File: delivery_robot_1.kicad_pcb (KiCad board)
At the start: 4 copper layers, 100 x 106 mm, 156 parts, among them J1 SWD, J13 Pi 5 link, J14 Pi 5 power, J15 Motor2 encoder, J16 MDD20A PWM2/DIR2/GND, J17 Latch servo, J18 AUX1 Notecard, J19 AUX2 LiDAR, J2 XT30PW-M, J20 AUX3 GNSS, J21 AUX4 IMU, J22 AUX force-on, J4 BOOT0 jumper, J5 Power test points, J6 MDD20A PWM1/DIR1/GND, J7 Motor1 encoder, J8 Expansion header, Q1 SQJ409EP, Q2 DMN63D8L, SW1 RESET, U1 STM32F091RCTx, U10 74LVC2G17, U11 USBLC6-2SC6, U12 USBLC6-2SC6, U2 TPSM63606RDLR, U3 TPS54202DDCR, U4 TPS7A8101DRBR, U5 TPSM63606RDLR, U6 USBLC6-2SC6, U7 USBLC6-2SC6, U8 SN74LVC1T45DBV, U9 74LVC2G17, Y3 8MHz

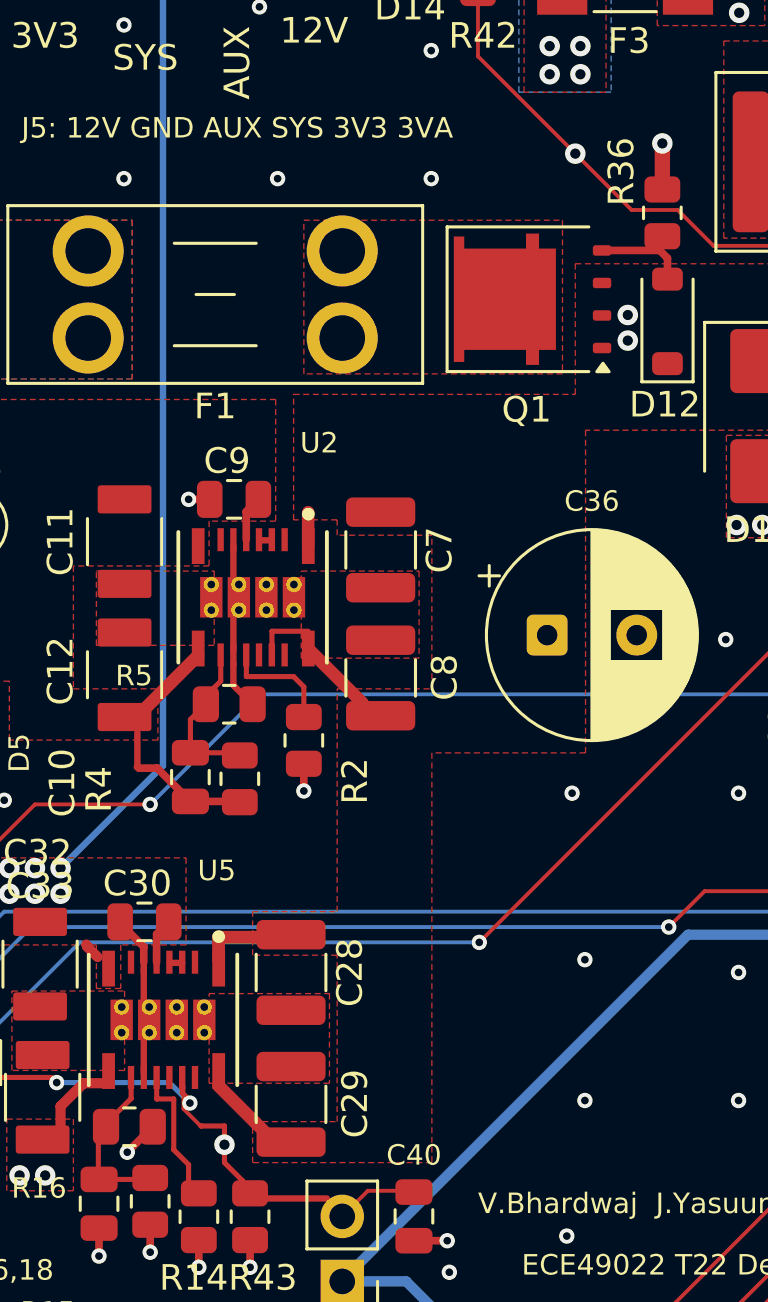
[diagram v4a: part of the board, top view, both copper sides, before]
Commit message: Widen high-current power paths for current capacity
- VBAT_FUSED pour (F1 -> Q1) raised to 8.6 mm and duplicated on B.Cu,
  with four 0.4 mm vias beside Q1; drop one GND via inside it.
- U2/U5 +12V input stubs widened from 0.5 mm to 1.0 mm.
- Thermal spokes on the VBAT_IN, VBAT_FUSED and +5V_PI pours widened
  from 1.0 mm to 1.5 mm.

Every power path now has at least 1.6x margin (IPC-2221, 10 C rise)
at simultaneous worst-case loads.
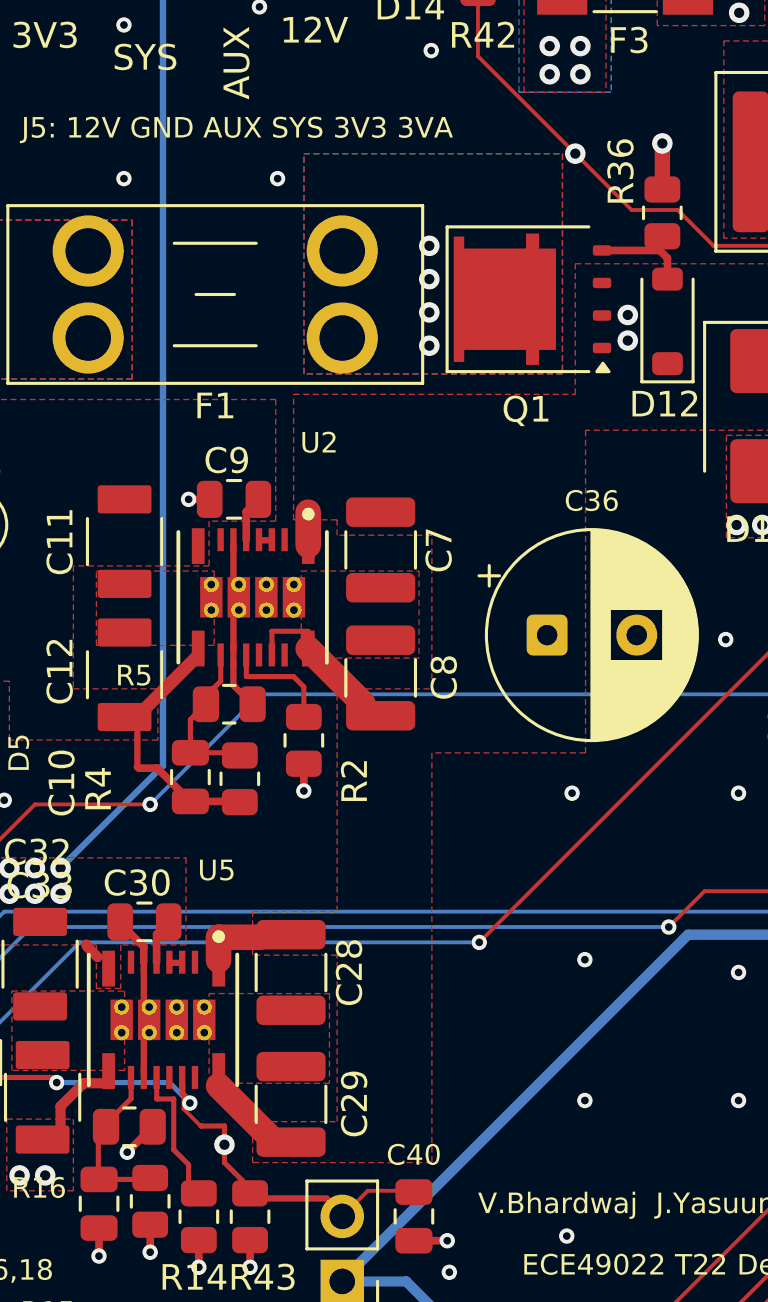
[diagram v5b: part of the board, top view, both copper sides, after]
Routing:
- net VBAT_FUSED: vias 0 -> 4
- net GND: vias 252 -> 251
- added copper zone on B.Cu, net VBAT_FUSED
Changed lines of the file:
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@@
 		(grid_origin 85 50)
 		(pcbplotparams
-			(layerselection 0x00000000_00000000_55555555_5755f5ff)
-			(plot_on_all_layers_selection 0x00000000_00000000_00000000_00000000)
+			(layerselection 0x00000000_00000000_55555555_57555555)
+			(plot_on_all_layers_selection 0x00000000_00000000_00000000_02000000)
 			(disableapertmacros no)
 			(usegerberextensions no)
@@
 			(psnegative no)
 			(psa4output no)
-			(plot_black_and_white yes)
+			(plot_black_and_white no)
 			(sketchpadsonfab no)
 			(plotpadnumbers no)
@@
 			(crossoutdnponfab yes)
 			(subtractmaskfromsilk no)
-			(outputformat 1)
+			(outputformat 5)
 			(mirror no)
-			(drillshape 1)
+			(drillshape 2)
 			(scaleselection 1)
-			(outputdirectory "")
+			(outputdirectory "plots/")
 		)
 	)
@@
 	)
 	(via
-		(at 117.975 70.975)
-		(size 0.6)
-		(drill 0.3)
-		(layers "F.Cu" "B.Cu")
-		(net "GND")
-	)
-	(via
 		(at 111.975 136.975)
 		(size 0.6)
@@
 		(start 109.67 106.4)
 		(end 111.6 108.33)
-		(width 0.5)
+		(width 1)
 		(layer "F.Cu")
 		(net "+12V")
@@
 		(start 109.67 100.6)
 		(end 111.3 100.6)
-		(width 0.5)
+		(width 1)
 		(layer "F.Cu")
 		(net "+12V")
@@
 		(start 113.17 89.33)
 		(end 115.3 91.46)
-		(width 0.49)
+		(width 1)
 		(layer "F.Cu")
 		(net "+12V")
@@
 		(start 109.67 101.5)
 		(end 109.67 100.6)
-		(width 0.5)
+		(width 1)
 		(layer "F.Cu")
 		(net "+12V")
@@
 		(start 113.17 85.3)
 		(end 113.17 84)
-		(width 0.49)
+		(width 1)
 		(layer "F.Cu")
 		(net "+12V")
@@
 		(net "/Input Protection/Q1_GATE")
 	)
+	(via
+		(at 117.9 77.5)
+		(size 0.8)
+		(drill 0.4)
+		(layers "F.Cu" "B.Cu")
+		(tenting
+			(front yes)
+			(back yes)
+		)
+		(net "VBAT_FUSED")
+	)
+	(via
+		(at 117.9 73.6)
+		(size 0.8)
+		(drill 0.4)
+		(layers "F.Cu" "B.Cu")
+		(tenting
+			(front yes)
+			(back yes)
+		)
+		(net "VBAT_FUSED")
+	)
+	(via
+		(at 117.9 74.9)
+		(size 0.8)
+		(drill 0.4)
+		(layers "F.Cu" "B.Cu")
+		(tenting
+			(front yes)
+			(back yes)
+		)
+		(net "VBAT_FUSED")
+	)
+	(via
+		(at 117.9 76.2)
+		(size 0.8)
+		(drill 0.4)
+		(layers "F.Cu" "B.Cu")
+		(tenting
+			(front yes)
+			(back yes)
+		)
+		(net "VBAT_FUSED")
+	)
 	(segment
 		(start 167.80433 119.794031)
@@
 	)
 	(zone
-		(net "VBAT_FUSED")
-		(layer "F.Cu")
-		(name "VBAT_FUSED")
-		(hatch edge 0.5)
-		(priority 5)
-		(connect_pads thru_hole_only
-			(clearance 0.5)
-		)
-		(min_thickness 0.25)
-		(fill yes
-			(thermal_gap 0.5)
-			(thermal_bridge_width 1)
-			(island_removal_mode 0)
-		)
-		(polygon
-			(pts
-				(xy 113 72.6) (xy 123.1 72.6) (xy 123.1 78.6) (xy 113 78.6)
-			)
-		)
-	)
-	(zone
 		(net "GND")
 		(layer "F.Cu")
@@
 		(fill yes
 			(thermal_gap 0.5)
-			(thermal_bridge_width 1)
+			(thermal_bridge_width 1.5)
 			(island_removal_mode 0)
 		)
@@
 		(fill yes
 			(thermal_gap 0.5)
-			(thermal_bridge_width 1)
+			(thermal_bridge_width 1.5)
 			(island_removal_mode 0)
 		)
@@
 			)
 		)
+	)
+	(zone
+		(net "VBAT_FUSED")
+		(layers "F.Cu" "B.Cu")
+		(name "VBAT_FUSED")
+		(hatch edge 0.5)
+		(priority 5)
+		(connect_pads thru_hole_only
+			(clearance 0.5)
+		)
+		(min_thickness 0.25)
+		(fill yes
+			(thermal_gap 0.5)
+			(thermal_bridge_width 1.5)
+			(island_removal_mode 0)
+		)
+		(polygon
+			(pts
+				(xy 113 70) (xy 123.1 70) (xy 123.1 78.6) (xy 113 78.6)
+			)
+		)

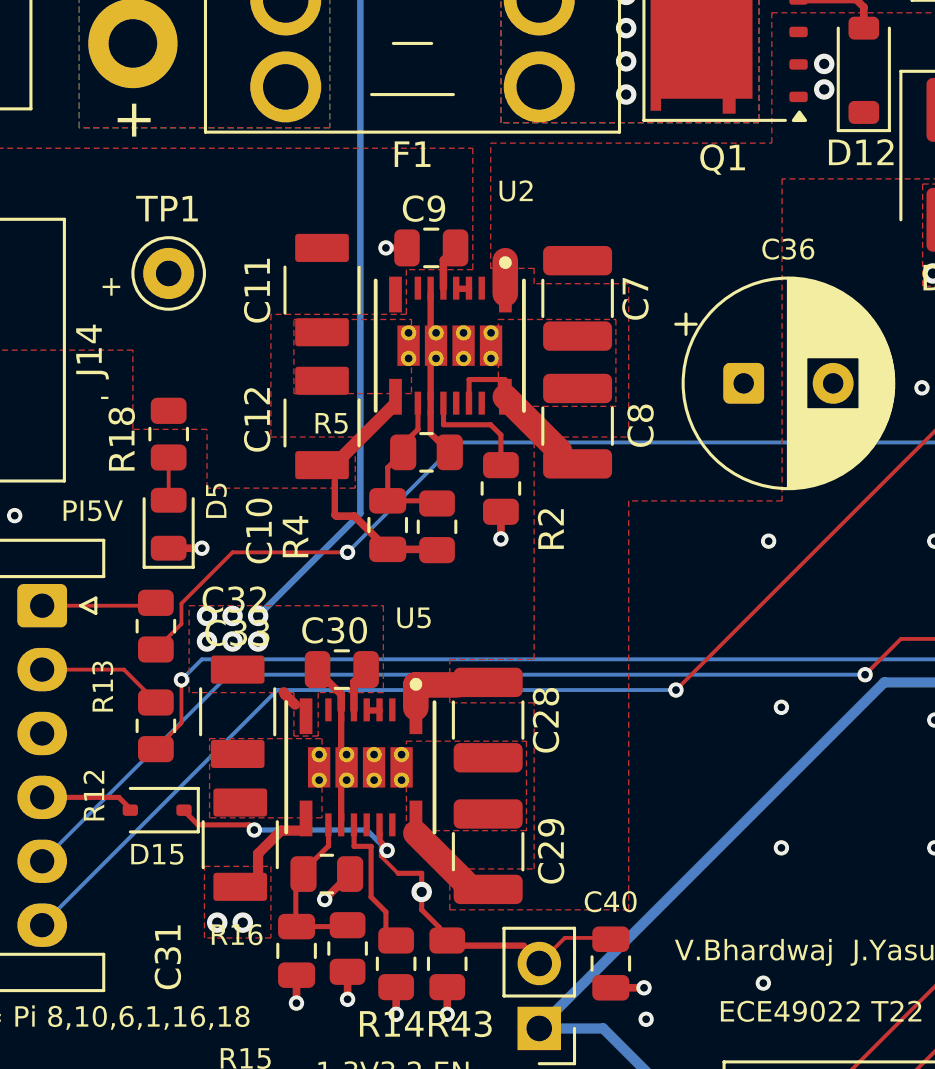
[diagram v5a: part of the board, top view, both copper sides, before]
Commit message: Apply TA layout feedback on regulator copper and In2
- Add 13 vias on U2's +5V_PI output (next to VOUT pins and C11/C12)
  into a new In2 +5V_PI area that mirrors the top pour.
- Mirror the regulator pours on In2: +12V under the input pours, GND
  under each module and its cap loops; add 15 +12V vias near
  C7/C8, C28/C29 and along the U5 feed.
- Fix the 12V choke points: In2 +12V neck at x=121 widened from
  1.5 to 7 mm; the top-layer feed to U5 widened from 3.5 to 4.7 mm
  with a 6.5 mm In2 path in parallel.
- Backfill In2 with a lowest-priority GND pour (62% -> 81% copper).
- Include the U2/U5 tented GND vias added earlier.
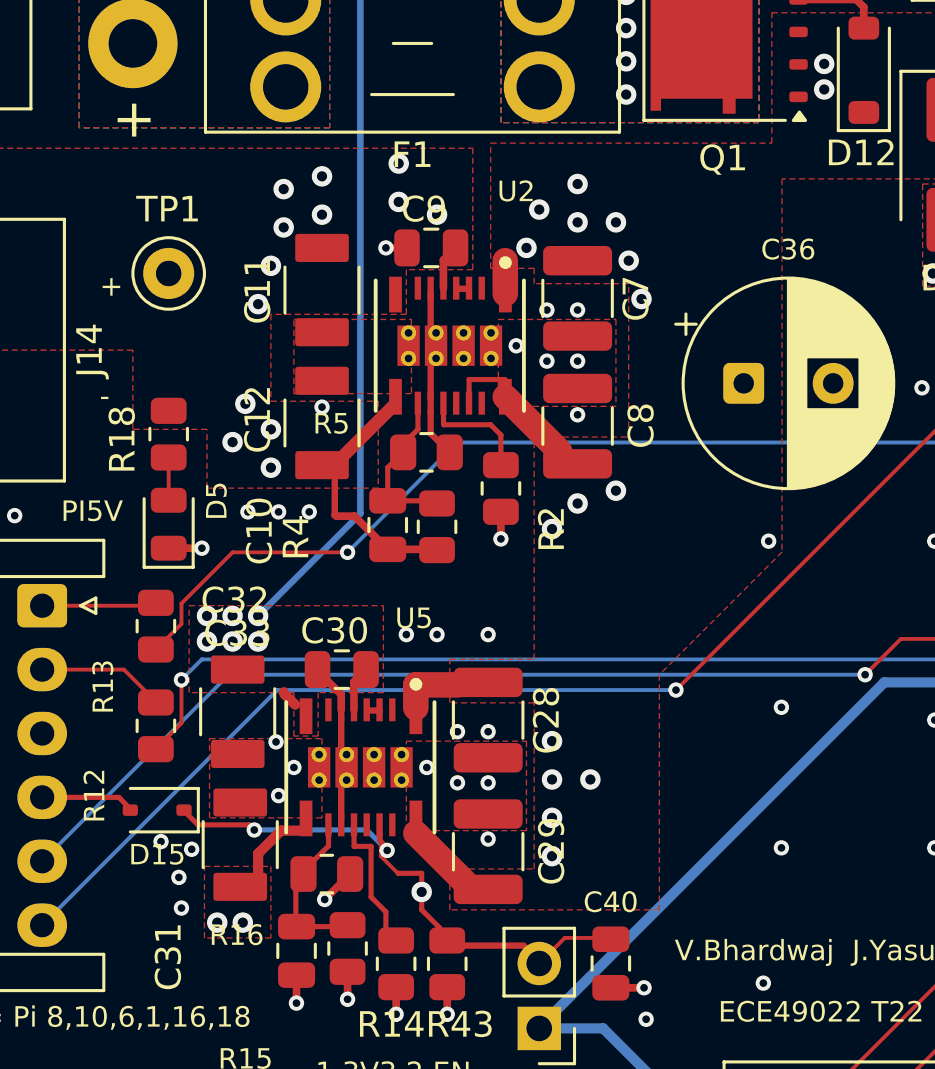
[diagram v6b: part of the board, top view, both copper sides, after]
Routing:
- net GND: vias 251 -> 277
- net +5V_PI: vias 0 -> 13
- net +12V: vias 14 -> 29
- added copper zone on In2.Cu, net +5V_PI
- added copper zone on In2.Cu, net GND
